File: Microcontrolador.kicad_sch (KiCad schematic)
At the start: 7 parts, among them U3 MIMXRT685SFVKB

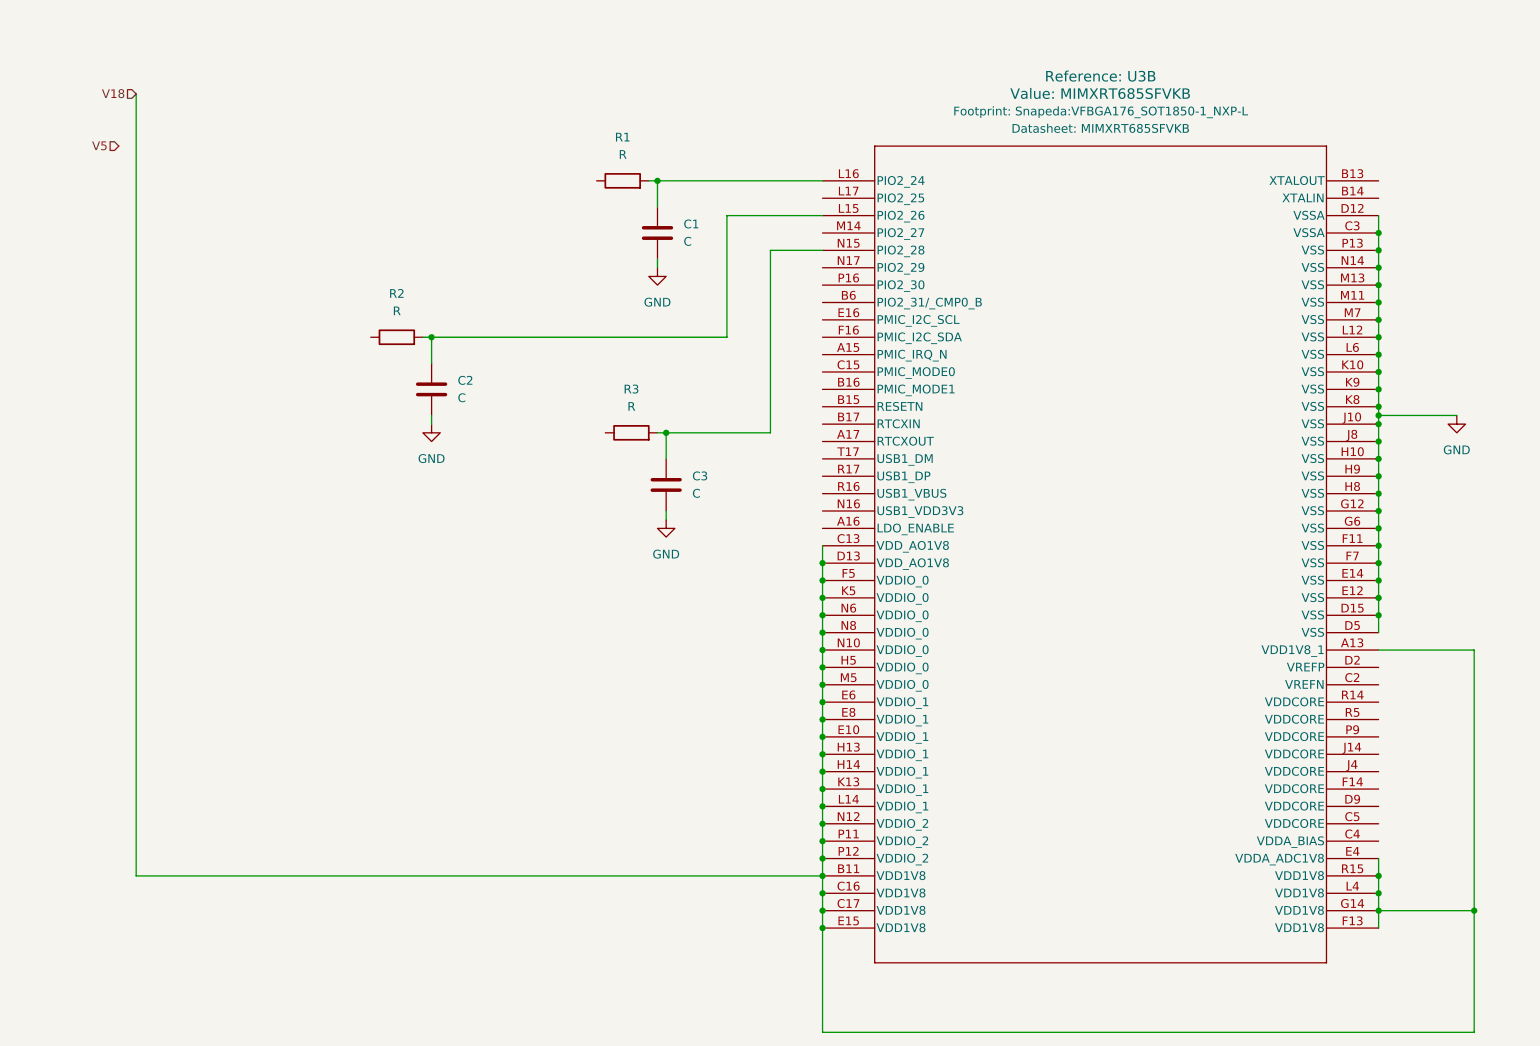
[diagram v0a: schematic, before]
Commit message: branch microcontrolador 1.1
Modificaciones iniciales de la subhoja del micro
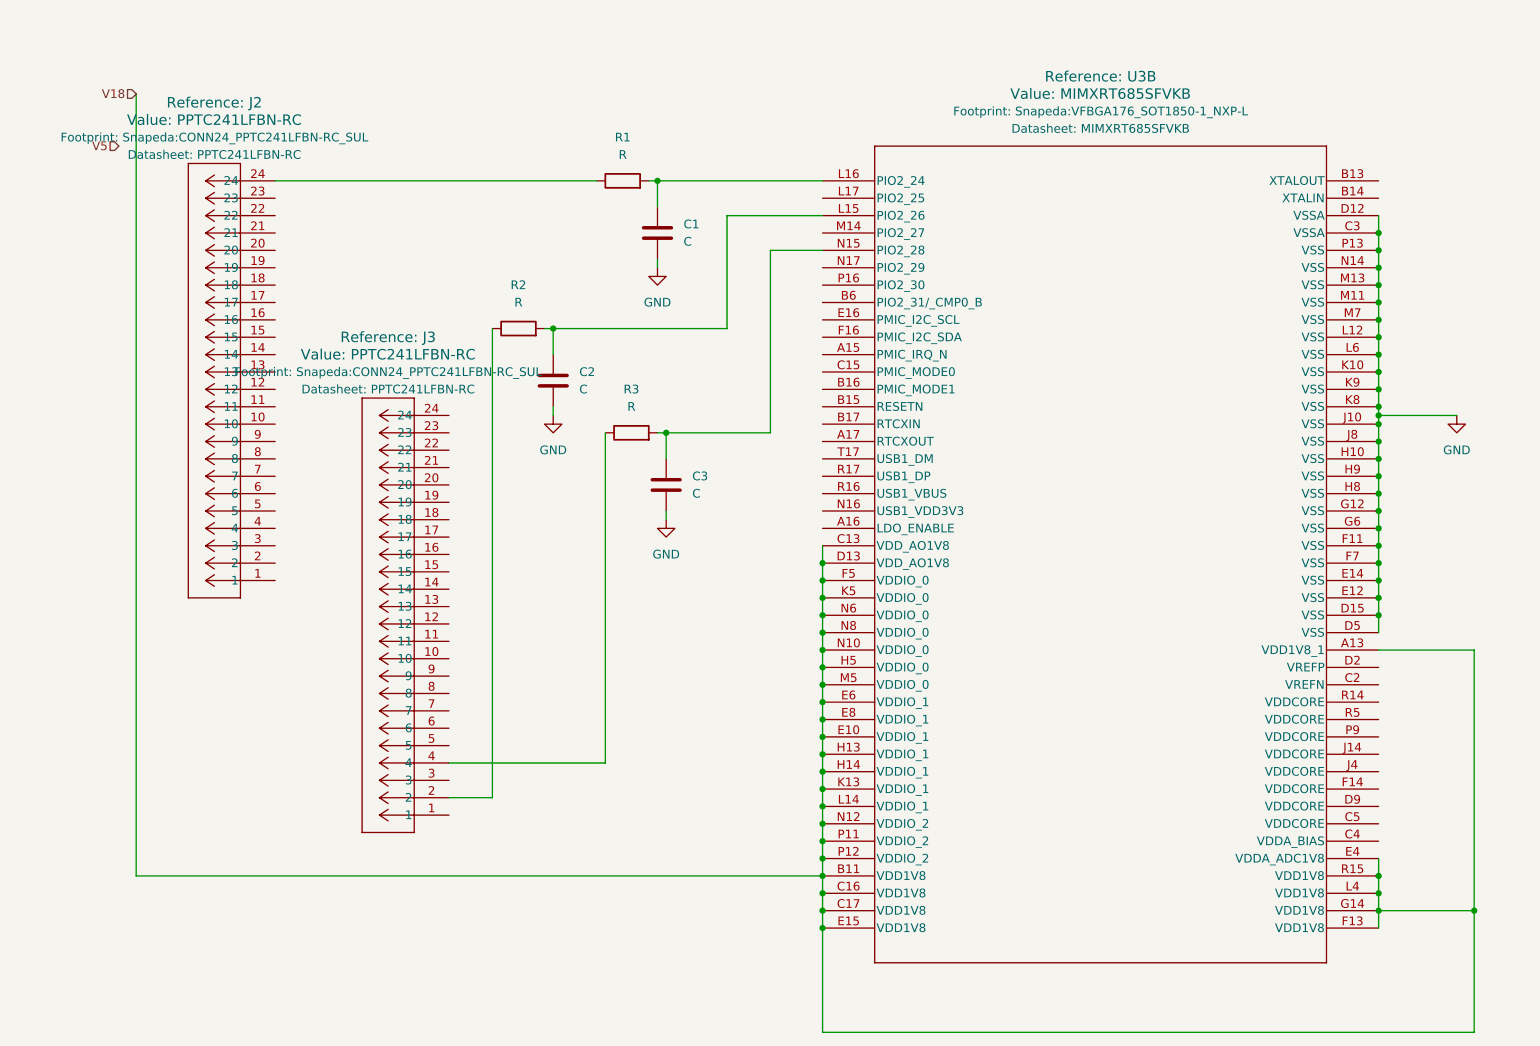
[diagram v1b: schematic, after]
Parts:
- added J2, J3: PPTC241LFBN-RC, Snapeda:CONN24_PPTC241LFBN-RC_SUL, symbol Snapeda:PPTC241LFBN-RC
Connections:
- net at R3.1: now also J3.4
- net at R2.1: now also J3.2
- net at R1.1: now also J2.24
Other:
- moved on the sheet: C2, R2

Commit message: branch microcontrolador  1.2
Completamos huellas y MPN
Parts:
- C1, C2, C3: value C -> 100n; footprint (none) -> Capacitor_SMD:C_01005_0402Metric; MPN (none) -> GRM188R71C104KA01D
- R1, R2, R3: value R -> 1k; footprint (none) -> Resistor_SMD:R_01005_0402Metric; MPN (none) -> RC0603FR-071KL
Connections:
- net at J3.4: now also R2.1; no longer R3.1
- net at C3.1, U3.N15 (PIO2_28): now also R2.2; no longer R3.2
- net at J3.2: now also R3.1; no longer R2.1
- net at C2.1, U3.L15 (PIO2_26): now also R3.2; no longer R2.2
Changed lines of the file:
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@@
 		(dnp no)
 		(fields_autoplaced yes)
-		(property "Reference" "R3"
+		(property "Reference" "R2"
 			(at 106.68 64.77 90)
 			(show_name no)
@@
 			)
 		)
-		(property "Value" "R"
+		(property "Value" "1k"
 			(at 106.68 67.31 90)
 			(show_name no)
@@
 			)
 		)
-		(property "Footprint" ""
+		(property "Footprint" "Resistor_SMD:R_01005_0402Metric"
 			(at 106.68 72.898 90)
 			(hide yes)
@@
 		(property "Description" "Resistor"
 			(at 106.68 71.12 0)
+			(hide yes)
+			(show_name no)
+			(do_not_autoplace no)
+			(effects
+				(font
+					(size 1.27 1.27)
+				)
+			)
+		)
+		(property "MPN" "RC0603FR-071KL"
+			(at 106.68 71.12 90)
 			(hide yes)
 			(show_name no)
@@
 			(project "Tarea_2"
 				(path "/9f5ae3b6-454f-40a7-b9eb-0aa1aaaab031/541a7019-0d72-4397-91e5-bb6aa7bc5984"
-					(reference "R3")
+					(reference "R2")
 					(unit 1)
 				)
@@
 	)
 	(symbol
-		(lib_id "Device:R")
-		(at 90.17 55.88 90)
+		(lib_id "Device:C")
+		(at 111.76 78.74 0)
 		(unit 1)
 		(body_style 1)
@@
 		(dnp no)
 		(fields_autoplaced yes)
-		(property "Reference" "R2"
-			(at 90.17 49.53 90)
-			(show_name no)
-			(do_not_autoplace no)
-			(effects
-				(font
-					(size 1.27 1.27)
-				)
-			)
-		)
-		(property "Value" "R"
-			(at 90.17 52.07 90)
-			(show_name no)
-			(do_not_autoplace no)
-			(effects
-				(font
-					(size 1.27 1.27)
-				)
-			)
-		)
-		(property "Footprint" ""
-			(at 90.17 57.658 90)
+		(property "Reference" "C3"
+			(at 115.57 77.4699 0)
+			(show_name no)
+			(do_not_autoplace no)
+			(effects
+				(font
+					(size 1.27 1.27)
+				)
+				(justify left)
+			)
+		)
+		(property "Value" "100n"
+			(at 115.57 80.0099 0)
+			(show_name no)
+			(do_not_autoplace no)
+			(effects
+				(font
+					(size 1.27 1.27)
+				)
+				(justify left)
+			)
+		)
+		(property "Footprint" "Capacitor_SMD:C_01005_0402Metric"
+			(at 112.7252 82.55 0)
 			(hide yes)
 			(show_name no)
@@
 		)
 		(property "Datasheet" ""
-			(at 90.17 55.88 0)
-			(hide yes)
-			(show_name no)
-			(do_not_autoplace no)
-			(effects
-				(font
-					(size 1.27 1.27)
-				)
-			)
-		)
-		(property "Description" "Resistor"
-			(at 90.17 55.88 0)
+			(at 111.76 78.74 0)
+			(hide yes)
+			(show_name no)
+			(do_not_autoplace no)
+			(effects
+				(font
+					(size 1.27 1.27)
+				)
+			)
+		)
+		(property "Description" "Unpolarized capacitor"
+			(at 111.76 78.74 0)
+			(hide yes)
+			(show_name no)
+			(do_not_autoplace no)
+			(effects
+				(font
+					(size 1.27 1.27)
+				)
+			)
+		)
+		(property "MPN" "GRM188R71C104KA01D"
+			(at 111.76 78.74 0)
 			(hide yes)
 			(show_name no)
@@
 			(project "Tarea_2"
 				(path "/9f5ae3b6-454f-40a7-b9eb-0aa1aaaab031/541a7019-0d72-4397-91e5-bb6aa7bc5984"
-					(reference "R2")
+					(reference "C3")
 					(unit 1)
 				)
@@
 			)
 		)
-		(property "Value" "R"
+		(property "Value" "1k"
 			(at 105.41 30.48 90)
 			(show_name no)
@@
 			)
 		)
-		(property "Footprint" ""
+		(property "Footprint" "Resistor_SMD:R_01005_0402Metric"
 			(at 105.41 36.068 90)
 			(hide yes)
@@
 		(property "Description" "Resistor"
 			(at 105.41 34.29 0)
+			(hide yes)
+			(show_name no)
+			(do_not_autoplace no)
+			(effects
+				(font
+					(size 1.27 1.27)
+				)
+			)
+		)
+		(property "MPN" "RC0603FR-071KL"
+			(at 105.41 34.29 90)
 			(hide yes)
 			(show_name no)
@@
 			)
 		)
-		(property "Value" "C"
+		(property "Value" "100n"
 			(at 114.3 43.1799 0)
 			(show_name no)
@@
 			)
 		)
-		(property "Footprint" ""
+		(property "Footprint" "Capacitor_SMD:C_01005_0402Metric"
 			(at 111.4552 45.72 0)
 			(hide yes)
@@
 		)
 		(property "Description" "Unpolarized capacitor"
+			(at 110.49 41.91 0)
+			(hide yes)
+			(show_name no)
+			(do_not_autoplace no)
+			(effects
+				(font
+					(size 1.27 1.27)
+				)
+			)
+		)
+		(property "MPN" "GRM188R71C104KA01D"
 			(at 110.49 41.91 0)
 			(hide yes)
@@
 				(path "/9f5ae3b6-454f-40a7-b9eb-0aa1aaaab031/541a7019-0d72-4397-91e5-bb6aa7bc5984"
 					(reference "C1")
+					(unit 1)
+				)
+			)
+		)
+	)
+	(symbol
+		(lib_id "Device:R")
+		(at 90.17 55.88 90)
+		(unit 1)
+		(body_style 1)
+		(exclude_from_sim no)
+		(in_bom yes)
+		(on_board yes)
+		(in_pos_files yes)
+		(dnp no)
+		(fields_autoplaced yes)
+		(property "Reference" "R3"
+			(at 90.17 49.53 90)
+			(show_name no)
+			(do_not_autoplace no)
+			(effects
+				(font
+					(size 1.27 1.27)
+				)
+			)
+		)
+		(property "Value" "1k"
+			(at 90.17 52.07 90)
+			(show_name no)
+			(do_not_autoplace no)
+			(effects
+				(font
+					(size 1.27 1.27)
+				)
+			)
+		)
+		(property "Footprint" "Resistor_SMD:R_01005_0402Metric"
+			(at 90.17 57.658 90)
+			(hide yes)
+			(show_name no)
+			(do_not_autoplace no)
+			(effects
+				(font
+					(size 1.27 1.27)
+				)
+			)
+		)
+		(property "Datasheet" ""
+			(at 90.17 55.88 0)
+			(hide yes)
+			(show_name no)
+			(do_not_autoplace no)
+			(effects
+				(font
+					(size 1.27 1.27)
+				)
+			)
+		)
+		(property "Description" "Resistor"
+			(at 90.17 55.88 0)
+			(hide yes)
+			(show_name no)
+			(do_not_autoplace no)
+			(effects
+				(font
+					(size 1.27 1.27)
+				)
+			)
+		)
+		(property "MPN" "RC0603FR-071KL"
+			(at 90.17 55.88 90)
+			(hide yes)
+			(show_name no)
+			(do_not_autoplace no)
+			(effects
+				(font
+					(size 1.27 1.27)
+				)
+			)
+		)
+		(pin "2"
+		)
+		(pin "1"
+		)
+		(instances
+			(project "Tarea_2"
+				(path "/9f5ae3b6-454f-40a7-b9eb-0aa1aaaab031/541a7019-0d72-4397-91e5-bb6aa7bc5984"
+					(reference "R3")
 					(unit 1)
 				)
@@
 			)
 		)
-		(property "Value" "C"
+		(property "Value" "100n"
 			(at 99.06 64.7699 0)
 			(show_name no)
@@
 			)
 		)
-		(property "Footprint" ""
+		(property "Footprint" "Capacitor_SMD:C_01005_0402Metric"
 			(at 96.2152 67.31 0)
 			(hide yes)
@@
 		)
 		(property "Description" "Unpolarized capacitor"
+			(at 95.25 63.5 0)
+			(hide yes)
+			(show_name no)
+			(do_not_autoplace no)
+			(effects
+				(font
+					(size 1.27 1.27)
+				)
+			)
+		)
+		(property "MPN" "GRM188R71C104KA01D"
 			(at 95.25 63.5 0)
 			(hide yes)
@@
 					(unit 1)
 				)
-			)
-		)
-	)
-	(symbol
-		(lib_id "Device:C")
-		(at 111.76 78.74 0)
-		(unit 1)
-		(body_style 1)
-		(exclude_from_sim no)
-		(in_bom yes)
-		(on_board yes)
-		(in_pos_files yes)
-		(dnp no)
-		(fields_autoplaced yes)
-		(property "Reference" "C3"
-			(at 115.57 77.4699 0)
-			(show_name no)
-			(do_not_autoplace no)
-			(effects
-				(font
-					(size 1.27 1.27)
-				)
-				(justify left)
-			)
-		)
-		(property "Value" "C"
-			(at 115.57 80.0099 0)
-			(show_name no)
-			(do_not_autoplace no)
-			(effects
-				(font
-					(size 1.27 1.27)
-				)
-				(justify left)
-			)
-		)
-		(property "Footprint" ""
-			(at 112.7252 82.55 0)
-			(hide yes)
-			(show_name no)
-			(do_not_autoplace no)
-			(effects
-				(font
-					(size 1.27 1.27)
-				)
-			)
-		)
-		(property "Datasheet" ""
-			(at 111.76 78.74 0)
-			(hide yes)
-			(show_name no)
-			(do_not_autoplace no)
-			(effects
-				(font
-					(size 1.27 1.27)
-				)
-			)
-		)
-		(property "Description" "Unpolarized capacitor"
-			(at 111.76 78.74 0)
-			(hide yes)
-			(show_name no)
-			(do_not_autoplace no)
-			(effects
-				(font
-					(size 1.27 1.27)
-				)
-			)
-		)
-		(pin "2"
-		)
-		(pin "1"
-		)
-		(instances
-			(project "Tarea_2"
-				(path "/9f5ae3b6-454f-40a7-b9eb-0aa1aaaab031/541a7019-0d72-4397-91e5-bb6aa7bc5984"
-					(reference "C3")
-					(unit 1)
-				)

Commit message: Microcontrolador 1.3
Completamos los MPN de los elementos de digikey
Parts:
- J2, J3: MPN (none) -> PPTC241LFBN-RC
- U3: MPN (none) -> MIMXRT685SFVKB
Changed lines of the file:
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@@
+			)
+		)
+		(property "MPN" "PPTC241LFBN-RC"
+			(at 80.01 127 0)
+			(hide yes)
+			(show_name no)
+			(do_not_autoplace no)
+			(effects
+				(font
+					(size 1.27 1.27)
+				)
 			)
 		)
@@
 			)
 		)
+		(property "MPN" "PPTC241LFBN-RC"
+			(at 54.61 92.71 0)
+			(hide yes)
+			(show_name no)
+			(do_not_autoplace no)
+			(effects
+				(font
+					(size 1.27 1.27)
+				)
+			)
+		)
 		(pin "6"
 		)
@@
 			(do_not_autoplace no)
 			(effects
+				(font
+					(size 1.27 1.27)
+				)
+			)
+		)
+		(property "MPN" "MIMXRT685SFVKB"
+			(at 134.62 34.29 0)
+			(hide yes)
+			(show_name no)
+			(do_not_autoplace no)
+			(effects

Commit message: - Primer commit de la rama
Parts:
- removed J2: PPTC241LFBN-RC, Snapeda:CONN24_PPTC241LFBN-RC_SUL, symbol Snapeda:PPTC241LFBN-RC
- added C7: 4.7u, Capacitor_SMD:C_01005_0402Metric, symbol Device:C
- added R5: 10k, symbol Device:R
- added R6: 100k, symbol Device:R
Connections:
- net GND: now also U3.A16 (LDO_ENABLE), U3.B14 (XTALIN), U3.B17 (RTCXIN), U3.C2 (VREFN), C7.2
- net V18: now also U3.C4 (VDDA_BIAS), U3.C5 (VDDCORE), U3.D2 (VREFP), U3.D9 (VDDCORE), U3.F14 (VDDCORE), U3.J14 (VDDCORE), U3.J4 (VDDCORE), U3.P9 (VDDCORE), U3.R14 (VDDCORE), U3.R5 (VDDCORE), C7.1, R5.2, R6.2
- net at R2.1: now also J3.22; no longer J3.4
- net at C3.1, R2.2: now also U3.L15 (PIO2_26); no longer U3.N15 (PIO2_28)
- net at J3.2: no longer R3.1
- net at J3.23: now also R3.1
- net at J3.24: now also R1.1
- net at C2.1, R3.2: now also U3.L17 (PIO2_25); no longer U3.L15 (PIO2_26)
- net at U3.A15 (PMIC_IRQ_N): now also R5.1
- net at U3.B15 (RESETN): now also R6.1
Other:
- moved on the sheet: Reference: J3
